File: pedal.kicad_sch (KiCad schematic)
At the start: 0 parts

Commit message: Added microcontroller and custom symbol library
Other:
- added sheet microcontroller (microcontroller.kicad_sch)
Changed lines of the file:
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@@
 	(generator_version "10.0")
 	(paper "A4")
+	(sheet
+		(at 72.39 72.39)
+		(size 21.59 10.16)
+		(exclude_from_sim no)
+		(in_bom yes)
+		(on_board yes)
+		(dnp no)
+		(fields_autoplaced yes)
+		(stroke
+			(width 0.1524)
+			(type solid)
+		)
+		(fill
+			(color 0 0 0 0)
+		)
+		(property "Sheetname" "microcontroller"
+			(at 72.39 71.6784 0)
+			(show_name no)
+			(do_not_autoplace no)
+			(effects
+				(font
+					(size 1.27 1.27)
+				)
+				(justify left bottom)
+			)
+		)
+		(property "Sheetfile" "microcontroller.kicad_sch"
+			(at 72.39 83.1346 0)
+			(show_name no)
+			(do_not_autoplace no)
+			(effects
+				(font
+					(size 1.27 1.27)
+				)
+				(justify left top)
+			)
+		)
+		(instances
+			(project "pedal"
+				(path "/e2443317-b83f-4e66-ac79-3186c6d613f3"
+					(page "2")
+				)
+			)
+		)
+	)
 	(sheet_instances
 		(path "/"

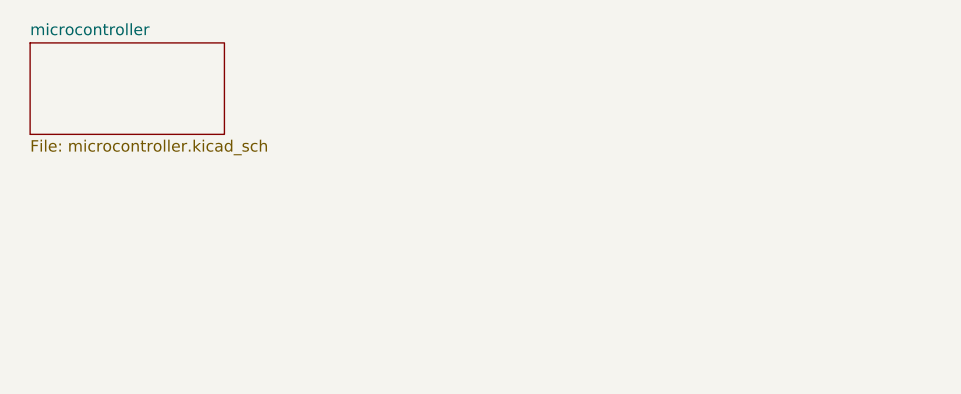
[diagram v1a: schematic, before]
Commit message: Power path (#1)
* add power path sheet

* Added TPS631000

* add-symbol.py now removes symbol files

* fixed microcontroller footprint

* buck boost regulator schematic done

* added LDO for LCD rail

* add tps2121 power mux component

* wip

* saved everything

* remove tps2121

* fix removing merged library files

* random silly commit

* add type c receptacle

* add esd protection to usb port

* add bq25302 charger

* charger supporting circuitry

* add fuel gauge

* fix fuel gauge symbol pins

* fuel gauge wip

* add switch for 3V3 enable

* vbatt is switched into power mux

* add switch model

* add pull up/down to fuel gauge

* LDO NC pin to ground

* formatting

* add display footprint

* embed 3d model for fuel gauge in footprint

* add switch switch to user drawings

* random changes

* rename custom libraries to custom, add easyeda2kicad integration

* embed all 3d models

* move switch to be on grid

* move stuff a bit

* add thermistor biasing resistors

* add battery connector

* update fast charge current

* update pcb

* add battery connector model and charge led

* replace battery connector with solder pads
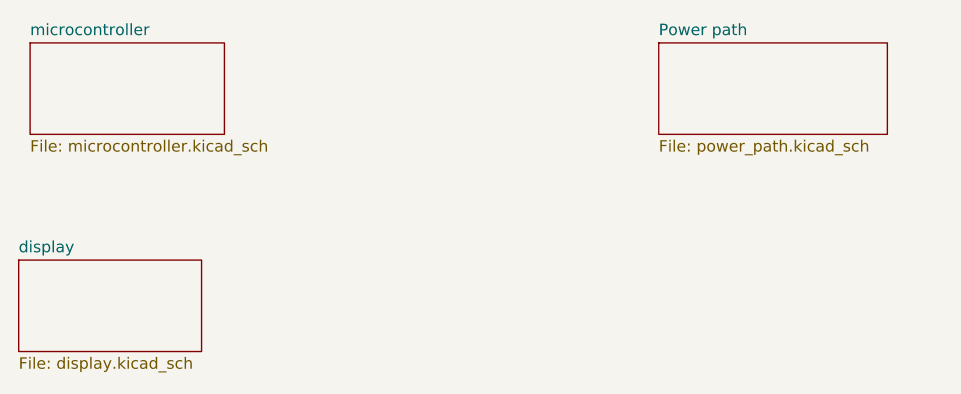
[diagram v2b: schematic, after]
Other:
- added sheet Power path (power_path.kicad_sch)
- added sheet display (display.kicad_sch)
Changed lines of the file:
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@@
 	(paper "A4")
+	(sheet
+		(at 142.24 72.39)
+		(size 25.4 10.16)
+		(exclude_from_sim no)
+		(in_bom yes)
+		(on_board yes)
+		(dnp no)
+		(fields_autoplaced yes)
+		(stroke
+			(width 0.1524)
+			(type solid)
+		)
+		(fill
+			(color 0 0 0 0)
+		)
+		(property "Sheetname" "Power path"
+			(at 142.24 71.6784 0)
+			(show_name no)
+			(do_not_autoplace no)
+			(effects
+				(font
+					(size 1.27 1.27)
+				)
+				(justify left bottom)
+			)
+		)
+		(property "Sheetfile" "power_path.kicad_sch"
+			(at 142.24 83.1346 0)
+			(show_name no)
+			(do_not_autoplace no)
+			(effects
+				(font
+					(size 1.27 1.27)
+				)
+				(justify left top)
+			)
+		)
+		(instances
+			(project "pedal"
+				(path "/e2443317-b83f-4e66-ac79-3186c6d613f3"
+					(page "3")
+				)
+			)
+		)
+	)
 	(sheet
 		(at 72.39 72.39)
@@
 				)
 			)
+		)
+	)
+	(sheet
+		(at 71.12 96.52)
+		(size 20.32 10.16)
+		(exclude_from_sim no)
+		(in_bom yes)
+		(on_board yes)
+		(dnp no)
+		(fields_autoplaced yes)
+		(stroke
+			(width 0.1524)
+			(type solid)
+		)
+		(fill
+			(color 0 0 0 0)
+		)
+		(property "Sheetname" "display"
+			(at 71.12 95.8084 0)
+			(show_name no)
+			(do_not_autoplace no)
+			(effects
+				(font
+					(size 1.27 1.27)
+				)
+				(justify left bottom)
+			)
+		)
+		(property "Sheetfile" "display.kicad_sch"
+			(at 71.12 107.2646 0)
+			(show_name no)
+			(do_not_autoplace no)
+			(effects
+				(font
+					(size 1.27 1.27)
+				)
+				(justify left top)
+			)
+		)
+		(instances
+			(project "pedal"
+				(path "/e2443317-b83f-4e66-ac79-3186c6d613f3"
+					(page "4")
+				)
+			)

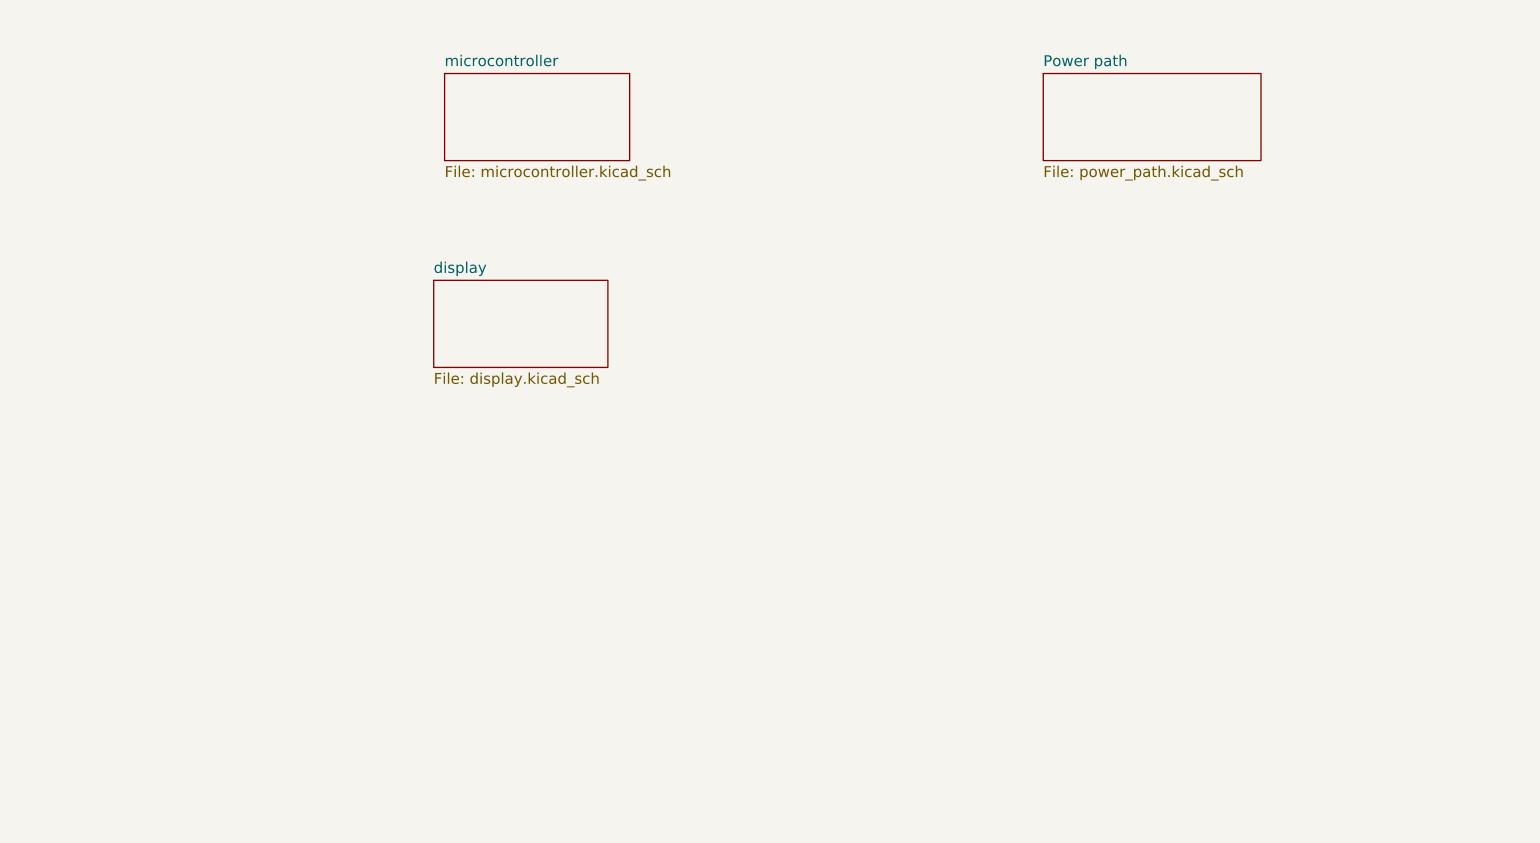
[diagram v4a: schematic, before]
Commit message: add imu sheet and library
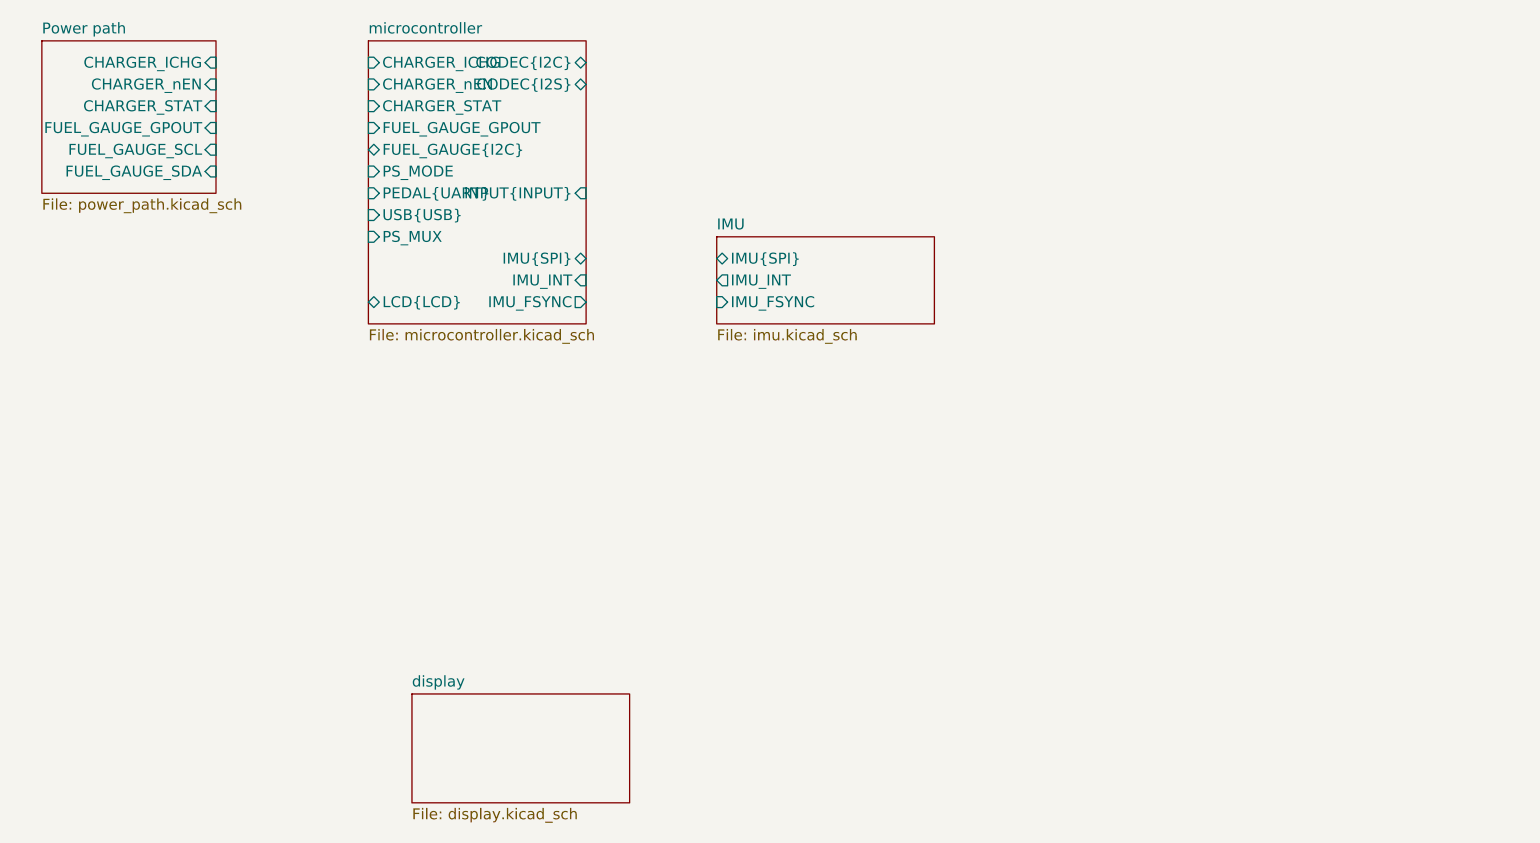
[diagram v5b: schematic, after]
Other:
- added sheet IMU (imu.kicad_sch)
- sheet Power path ports: added CHARGER_ICHG, CHARGER_STAT, CHARGER_nEN, FUEL_GAUGE_GPOUT, FUEL_GAUGE_SCL, FUEL_GAUGE_SDA; removed none
- sheet microcontroller ports: added CHARGER_ICHG, CHARGER_STAT, CHARGER_nEN, CODEC{I2C}, CODEC{I2S}, FUEL_GAUGE_GPOUT, FUEL_GAUGE{I2C}, IMU_FSYNC, IMU_INT, IMU{SPI}, INPUT{INPUT}, LCD{LCD}, PEDAL{UART}, PS_MODE, PS_MUX, USB{USB}; removed none

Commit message: fix up routing between sheets
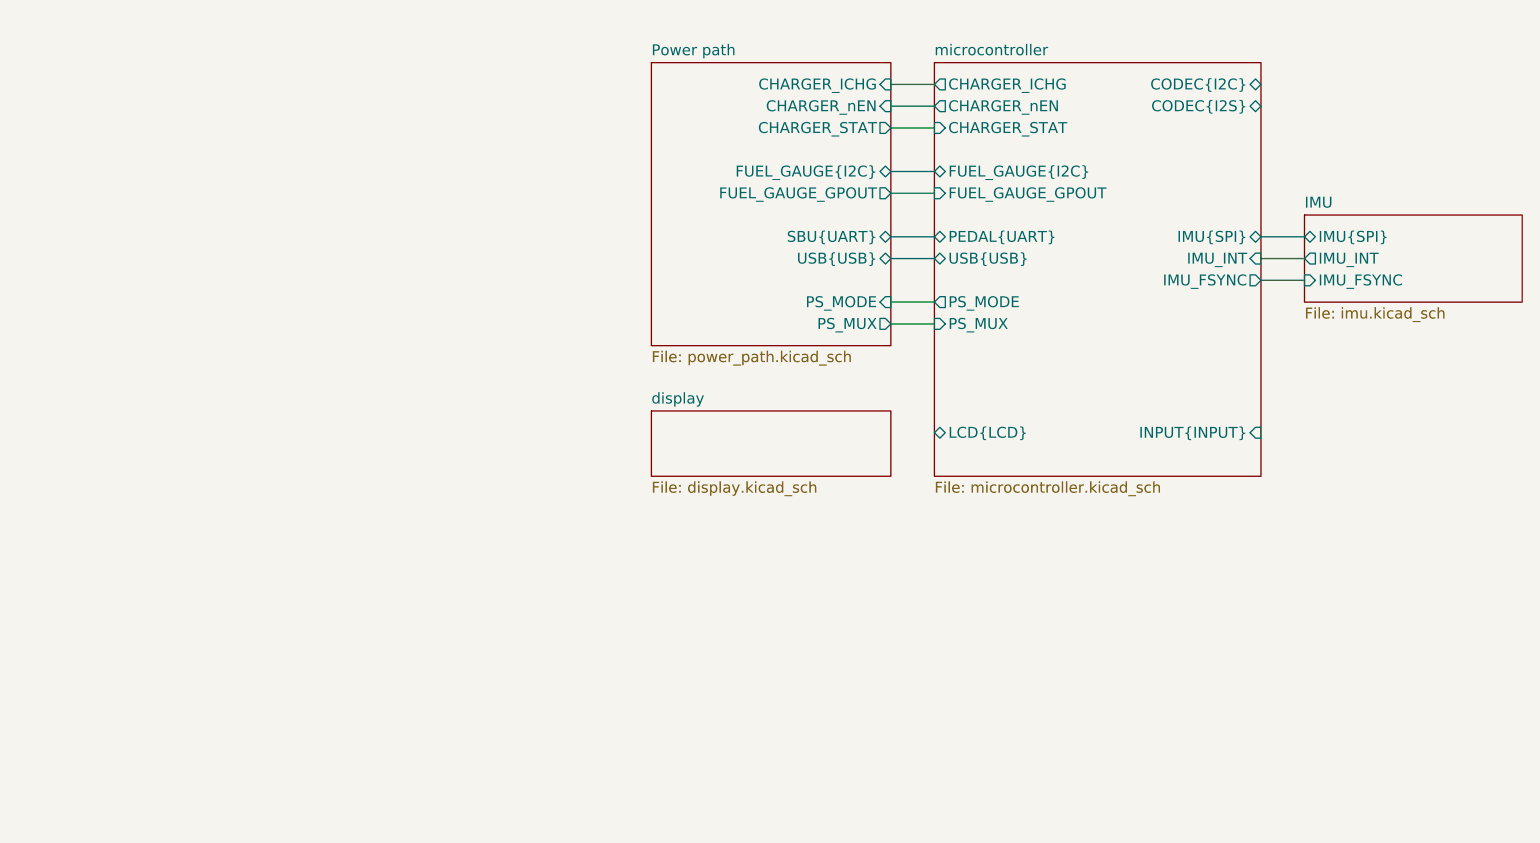
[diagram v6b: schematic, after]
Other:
- sheet Power path ports: added FUEL_GAUGE{I2C}, PS_MODE, PS_MUX, SBU{UART}, USB{USB}; removed FUEL_GAUGE_SCL, FUEL_GAUGE_SDA

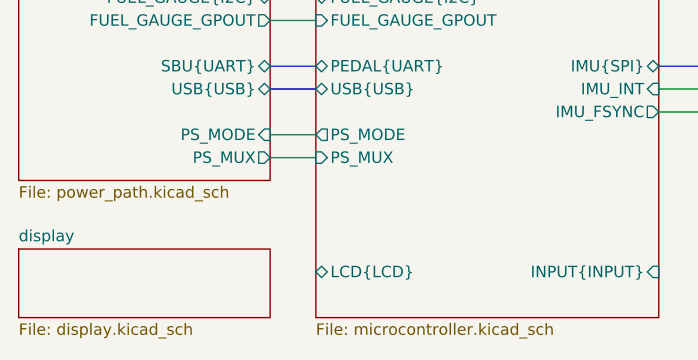
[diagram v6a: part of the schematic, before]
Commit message: add lcd backlight driver, hierarchical signals to display page
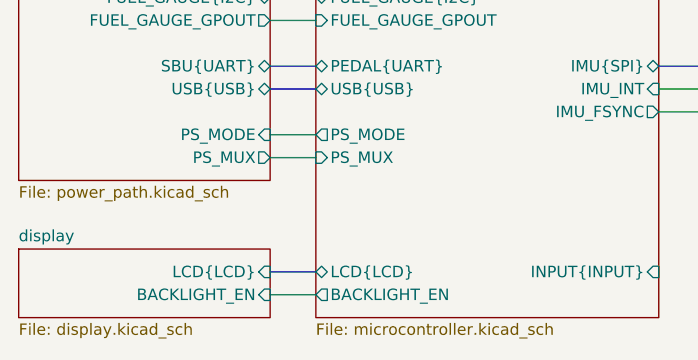
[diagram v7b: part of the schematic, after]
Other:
- sheet display ports: added BACKLIGHT_EN, LCD{LCD}; removed none
- sheet microcontroller ports: added BACKLIGHT_EN; removed none
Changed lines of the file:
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@@
+	(wire
+		(pts
+			(xy 124.46 116.84) (xy 129.54 116.84)
+		)
+		(stroke
+			(width 0)
+			(type default)
+		)
+	)
 	(wire
 		(pts
 			(xy 167.64 96.52) (xy 172.72 96.52)
+		)
+		(stroke
+			(width 0)
+			(type default)
+		)
+	)
+	(bus
+		(pts
+			(xy 124.46 114.3) (xy 129.54 114.3)
 		)
 		(stroke
@@
 			)
 		)
+		(pin "BACKLIGHT_EN" output
+			(at 129.54 116.84 180)
+			(effects
+				(font
+					(size 1.27 1.27)
+				)
+				(justify left)
+			)
+		)
 		(instances
 			(project "pedal"
@@
 			)
 		)
+		(pin "BACKLIGHT_EN" input
+			(at 124.46 116.84 0)
+			(effects
+				(font
+					(size 1.27 1.27)
+				)
+				(justify right)
+			)
+		)
+		(pin "LCD{LCD}" input
+			(at 124.46 114.3 0)
+			(effects
+				(font
+					(size 1.27 1.27)
+				)
+				(justify right)
+			)
+		)
